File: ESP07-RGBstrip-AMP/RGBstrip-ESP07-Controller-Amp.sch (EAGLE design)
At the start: 1 part

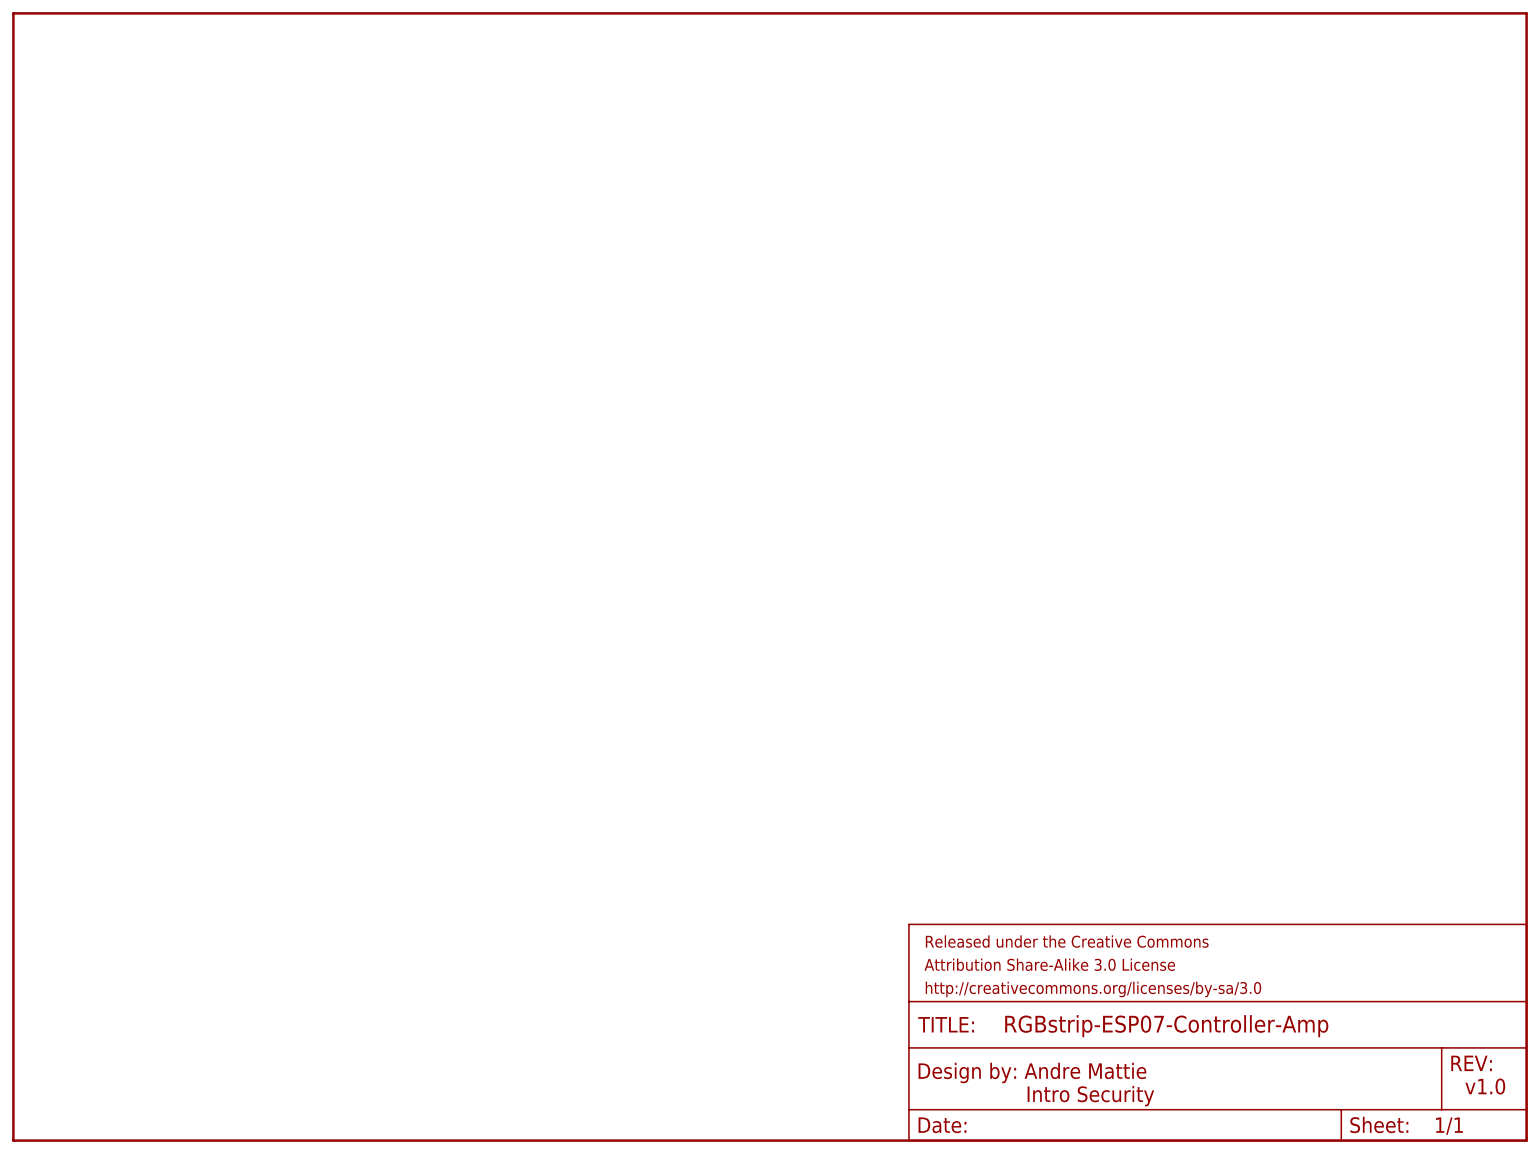
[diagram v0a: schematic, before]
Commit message: added new schematic and board for RGB LED controller/amplifier
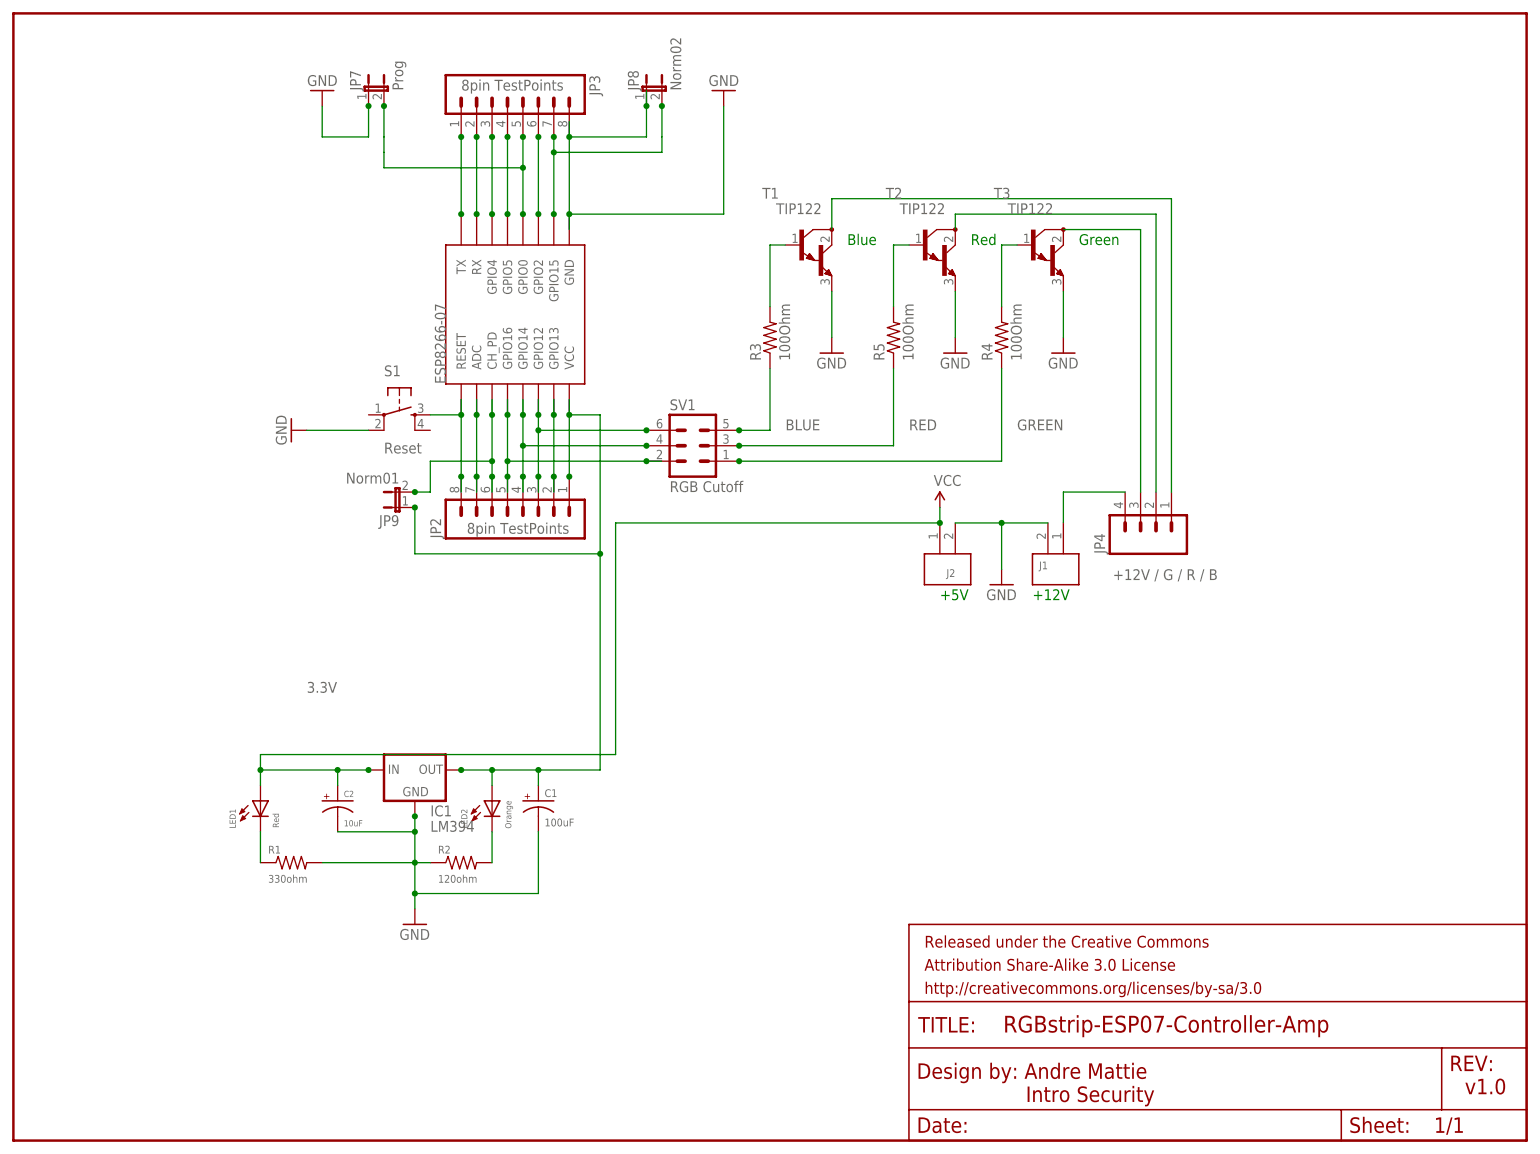
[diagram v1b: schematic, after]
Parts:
- added C1: 100uF, SparkFun-Capacitors:CAP_POLPTH1
- added C2: 10uF, SparkFun-Capacitors:CAP_POLPTH2
- added ESP8266-07: ESP07-16PIN, ESP8266:ESP07-16PIN
- added IC1: LM394, SparkFun-PowerIC:V_REG_78XXSINK
- added J1, J2: SCREW-TERMINAL_2_0.100, headers:SCREW-TERMINAL_2_0.100
- added JP2, JP3: 8pin TestPoints, SparkFun-Connectors:M08LONGPADS
- added JP4: +12V / G / R / B, SparkFun-Connectors:M04LONGPADS
- added JP7: Prog, jumper:JP1E
- added JP8: Norm02, jumper:JP1E
- added JP9: Norm01, jumper:JP1E
- added LED1: Red, adafruit:LED3MM
- added LED2: Orange, adafruit:LED3MM
- added R1: 330ohm, adafruit:R-US_0309/V
- added R2: 120ohm, adafruit:R-US_0309/V
- added R3, R4, R5: 100Ohm, SparkFun-Resistors:RESISTORPTH-1/4W
- added S1: Reset, SparkFun-Electromechanical:TAC_SWITCHPTH
- added SV1: RGB Cutoff, con-lstb:MA03-2
- added T1, T2, T3: TIP122, transistor:TIP122
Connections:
- new net 3.3V: C1.+, ESP8266-07.VCC, IC1.OUT, JP2.1, JP9.1, LED2.A
- new net BLUE: R3.1, SV1.5
- new net BLUE-SUPPLY: JP4.1, T1.C
- new net GND: C1.-, C2.-, ESP8266-07.GND, IC1.GND, J1.2, J2.2, JP3.8, JP7.1, JP8.1, R1.2, R2.1, S1.2, T1.E, T2.E, T3.E
- new net GREEN: R4.1, SV1.1
- new net GREEN-SUPPLY: JP4.3, T3.C
- new net N$10: R3.2, T1.B
- new net N$11: ESP8266-07.GPIO13, JP2.2
- new net N$12: ESP8266-07.GPIO15, JP3.7, JP8.2
- new net N$13: ESP8266-07.GPIO2, JP3.6
- new net N$14: ESP8266-07.GPIO0, JP3.5, JP7.2
- new net N$15: ESP8266-07.GPIO5, JP3.4
- new net N$16: ESP8266-07.GPIO4, JP3.3
- new net N$17: ESP8266-07.RX, JP3.2
- new net N$18: ESP8266-07.TX, JP3.1
- new net N$19: R5.2, T2.B
- new net N$20: J1.1, JP4.4
- new net N$21: R4.2, T3.B
- new net N$3: LED1.C, R1.1
- new net N$4: LED2.C, R2.2
- new net N$5: ESP8266-07.CH_PD, JP2.6, JP9.2
- new net N$6: ESP8266-07.ADC, JP2.7
- new net N$7: ESP8266-07.GPIO16, JP2.5, SV1.2
- new net N$8: ESP8266-07.GPIO14, JP2.4, SV1.4
- new net N$9: ESP8266-07.GPIO12, JP2.3, SV1.6
- new net RED: R5.1, SV1.3
- new net RED-SUPPLY: JP4.2, T2.C
- new net RESET: ESP8266-07.RESET, JP2.8, S1.3
- new net VCC: C2.+, IC1.IN, J2.1, LED1.A
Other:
- note added: "+12V"
- note added: "+5V"
- note added: "Blue"
- note added: "Green"
- note added: "Red"
